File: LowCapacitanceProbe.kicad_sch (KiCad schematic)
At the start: 21 parts, among them J1 u.Fl, J5 u.Fl, Q1 BF998, U1 SPX3819M5-L

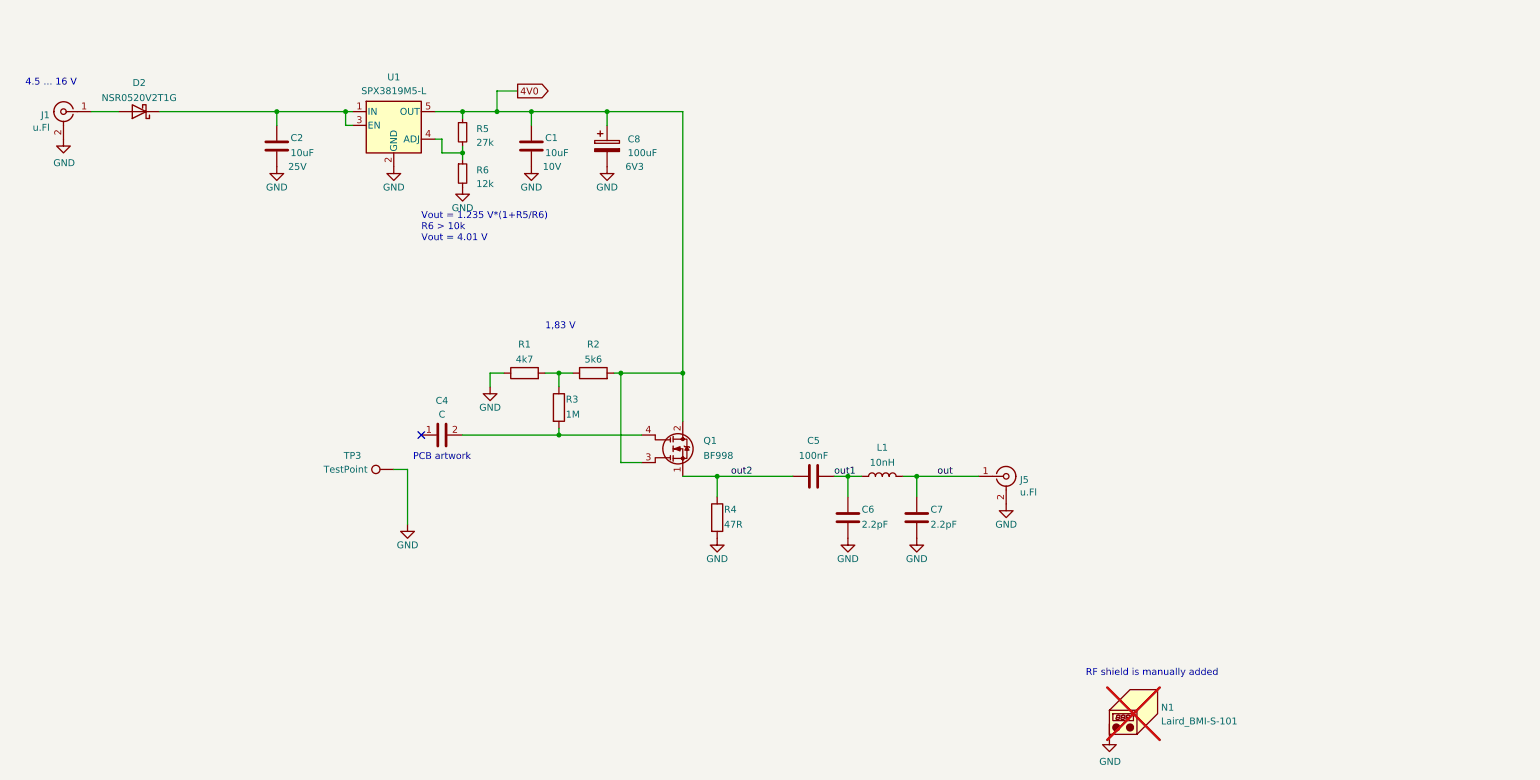
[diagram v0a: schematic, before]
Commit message: Slight fixes to simulation, started modifying schematics.
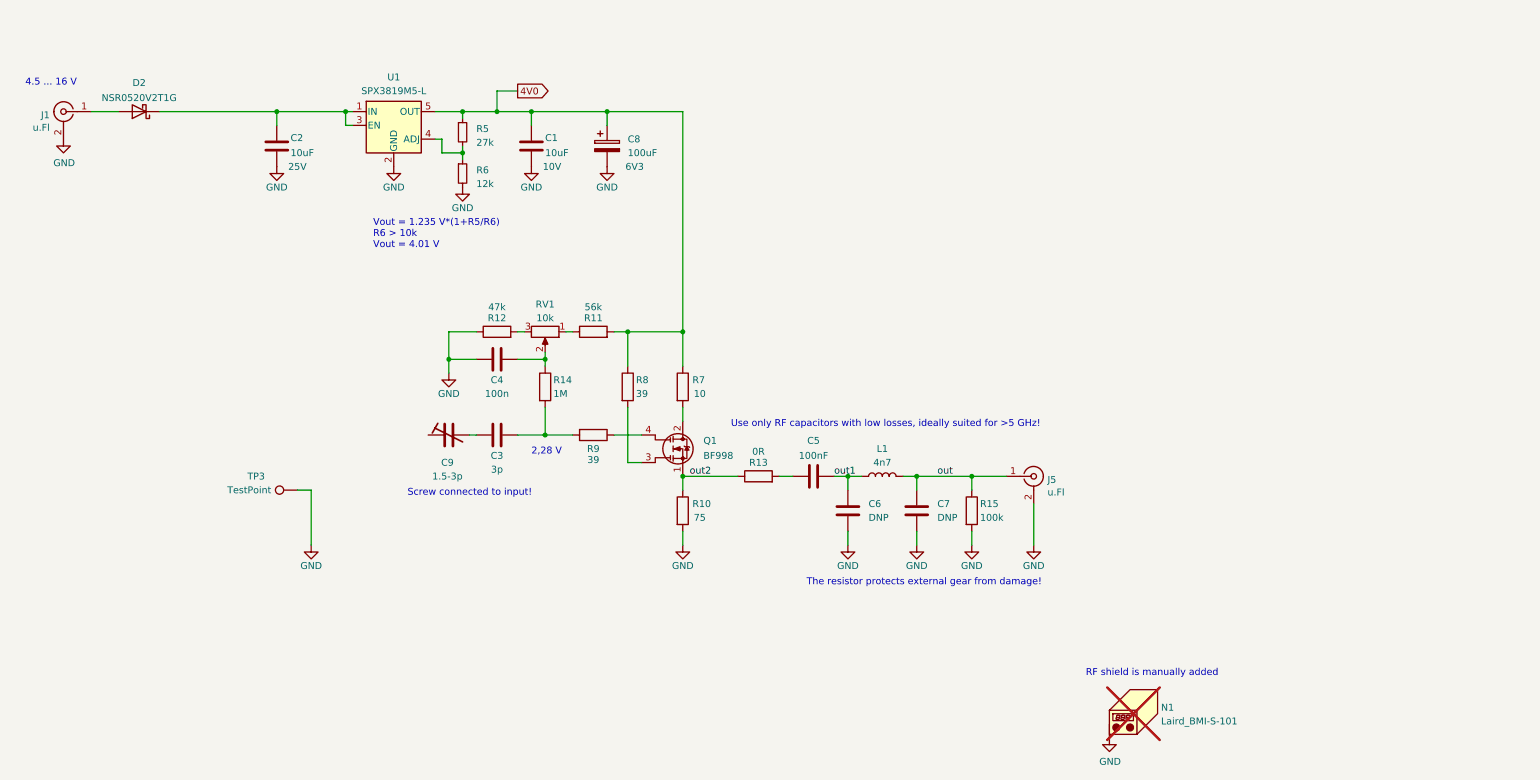
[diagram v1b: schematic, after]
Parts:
- removed R1: 4k7, Resistor_SMD:R_0402_1005Metric, symbol Device:R
- removed R2: 5k6, Resistor_SMD:R_0402_1005Metric, symbol Device:R
- removed R3: 1M, Resistor_SMD:R_0402_1005Metric, symbol Device:R
- removed R4: 47R, Resistor_SMD:R_0402_1005Metric, symbol Device:R
- added C3: 3p, symbol Device:C
- added C9: 1.5-3p, symbol Device:C_Trim
- added R10: 75, symbol Device:R
- added R11: 56k, symbol Device:R
- added R12: 47k, symbol Device:R
- added R13: 0R, symbol Device:R
- added R14: 1M, symbol Device:R
- added R15: 100k, symbol Device:R
- added R7: 10, symbol Device:R
- added R8, R9: 39, symbol Device:R
- added RV1: 10k, symbol Device:R_Potentiometer
- C4: value C -> 100n; footprint FETProbe:input_cap -> (none); now in the parts list
- C6, C7: value 2.2pF -> DNP; footprint FETProbe:C_0402_1005Metric_mod -> (none); LCSC Part C88927 -> (none); LCSC alternative C88887 -> (none); MPN RF15N2R2B500CT -> (none); OC_LCSC C172819 -> (none); dielectric NP0 -> (none)
- L1: value 10nH -> 4n7; footprint Inductor_SMD:L_0402_1005Metric -> (none); LCSC Part C90642 -> (none); MPN LQW15AN10NG80D -> (none)
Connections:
- net 4V0: now also R11.2, R7.1, R8.1; no longer Q1.2 (D), Q1.3 (G2)
- net GND: now also C4.2, R10.2, R12.1, R15.2
- net out: now also R15.1
- net out2: now also R10.1, R13.1; no longer C5.1
- net at Q1.4 (G1): now also R9.1; no longer C4.2
- net at C4.1: now also R14.1, RV1.2
- new net: C5.1, R13.2
- new net: Q1.2 (D), R7.2
- new net: Q1.3 (G2), R8.2
- new net: R11.1, RV1.1
- new net: R12.2, RV1.3
- new net: C3.1, C9.2
- new net: C3.2, R14.2, R9.2
- no-connect marks 1 -> 0
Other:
- note added: "2,28 V"
- note added: "Screw connected to input!"
- note added: "The resistor protects external gear from damage!"
- note added: "Use only RF capacitors with low losses, ideally suited for >5 GHz!"
- note removed: "1,83 V"
- note removed: "PCB artwork"
- moved on the sheet: J5, TP3

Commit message: Added more possibilities for tuning gain, added delinearization networks for easier fine-tuning, increased power supply voltage, fixed BF998 symbol. Added simulation of delinearization networks.
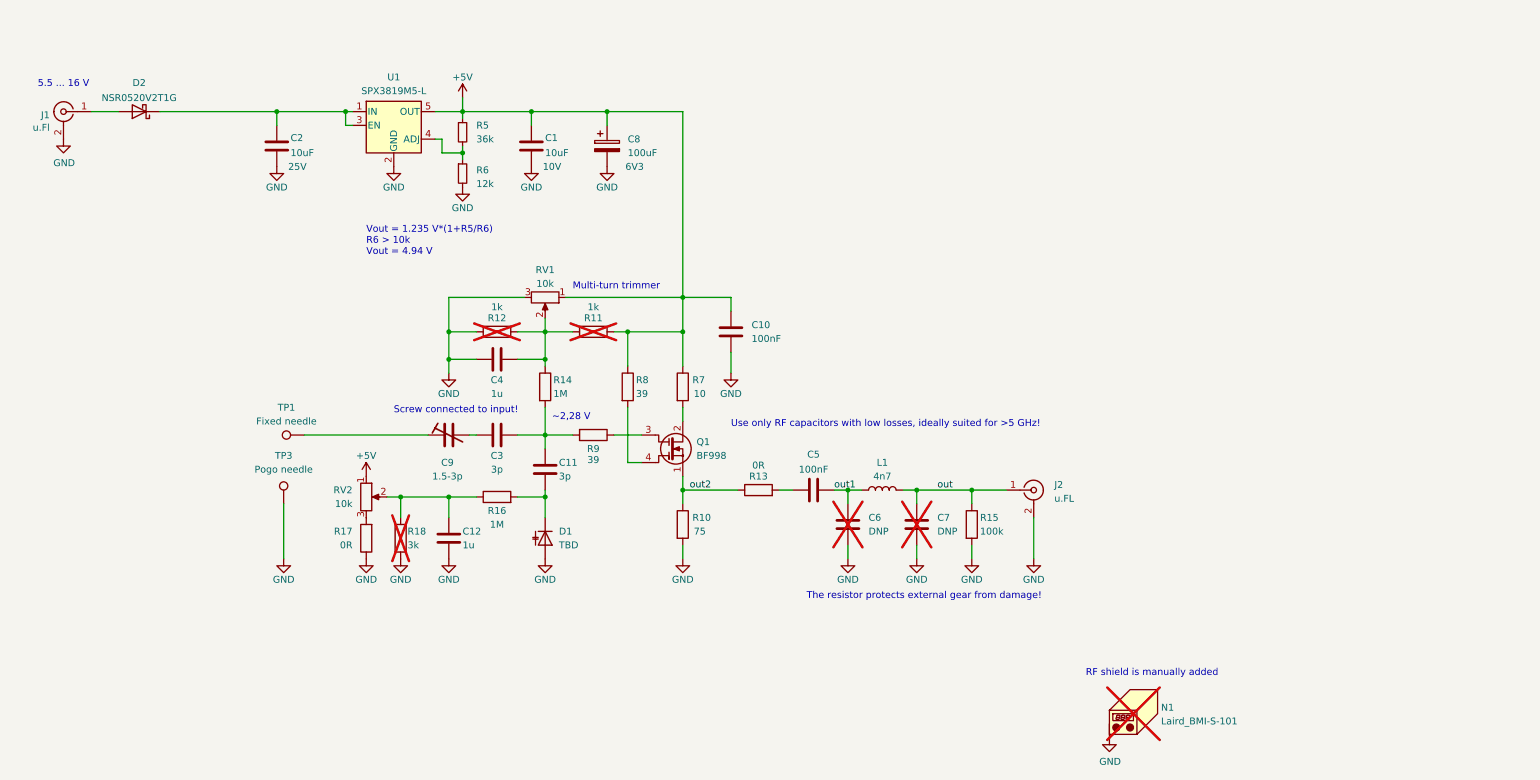
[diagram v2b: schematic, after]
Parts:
- removed J5: u.Fl, Connector_Coaxial:U.FL_Molex_MCRF_73412-0110_Vertical, symbol Connector:Conn_Coaxial
- removed Q1: BF998, FETProbe:SOT-143_mod, symbol BF998:BF998
- added C10: 100nF, Capacitor_SMD:C_1206_3216Metric, symbol Device:C
- added C11: 3p, symbol Device:C
- added C12: 1u, symbol Device:C
- added D1: TBD, symbol Device:D_Capacitance
- added J2: u.FL, Connector_Coaxial:U.FL_Molex_MCRF_73412-0110_Vertical, symbol petr:u.FL
- added Q1: BF998, Package_TO_SOT_SMD:SOT-143, symbol petr_kicad:BF998-petr_kicad_1
- added R16: 1M, symbol Device:R
- added R17: 0R, symbol Device:R
- added R18: 3k, symbol Device:R
- added RV2: 10k, symbol Device:R_Potentiometer
- added TP1: Fixed needle, symbol Connector:TestPoint
- C4: value 100n -> 1u
- C6, C7: now not fitted
- R11: value 56k -> 1k; now not fitted
- R12: value 47k -> 1k; now not fitted
- R5: value 27k -> 36k
- TP3: value TestPoint -> Pogo needle
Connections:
- net GND: now also RV1.3, C10.1, C12.2, D1.2 (A), J2.2 (Ext), R17.1, R18.1
- net out: now also J2.1 (In)
- net out2: now also Q1.1 (S)
- net at R7.2: now also Q1.2 (D)
- net at R8.2: now also Q1.4 (G2)
- net at R9.1: now also Q1.3 (G1)
- net at R11.1: now also C4.1, R12.2, R14.1, RV1.2; no longer RV1.1
- net at C3.2, R14.2, R9.2: now also C11.2
- net at C9.1: now also TP1.1
- net 4V0 renamed +5V
- net +5V: now also RV1.1, C10.2, RV2.1
- new net: C12.1, R16.1, R18.2, RV2.2
- new net: C11.1, D1.1 (K), R16.2
- new net: R17.2, RV2.3
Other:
- note added: "5.5 ... 16 V"
- note added: "Multi-turn trimmer"
- note added: "Vout = 1.235 V*(1+R5/R6) R6 > 10k Vout = 4.94 V"
- note added: "~2,28 V"
- note removed: "2,28 V"
- note removed: "4.5 ... 16 V"
- note removed: "Vout = 1.235 V*(1+R5/R6) R6 > 10k Vout = 4.01 V"
- moved on the sheet: C5, L1, R10, R13, R15, RV1, TP3

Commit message: Added calibration notes, fixed delinearization for gate bias
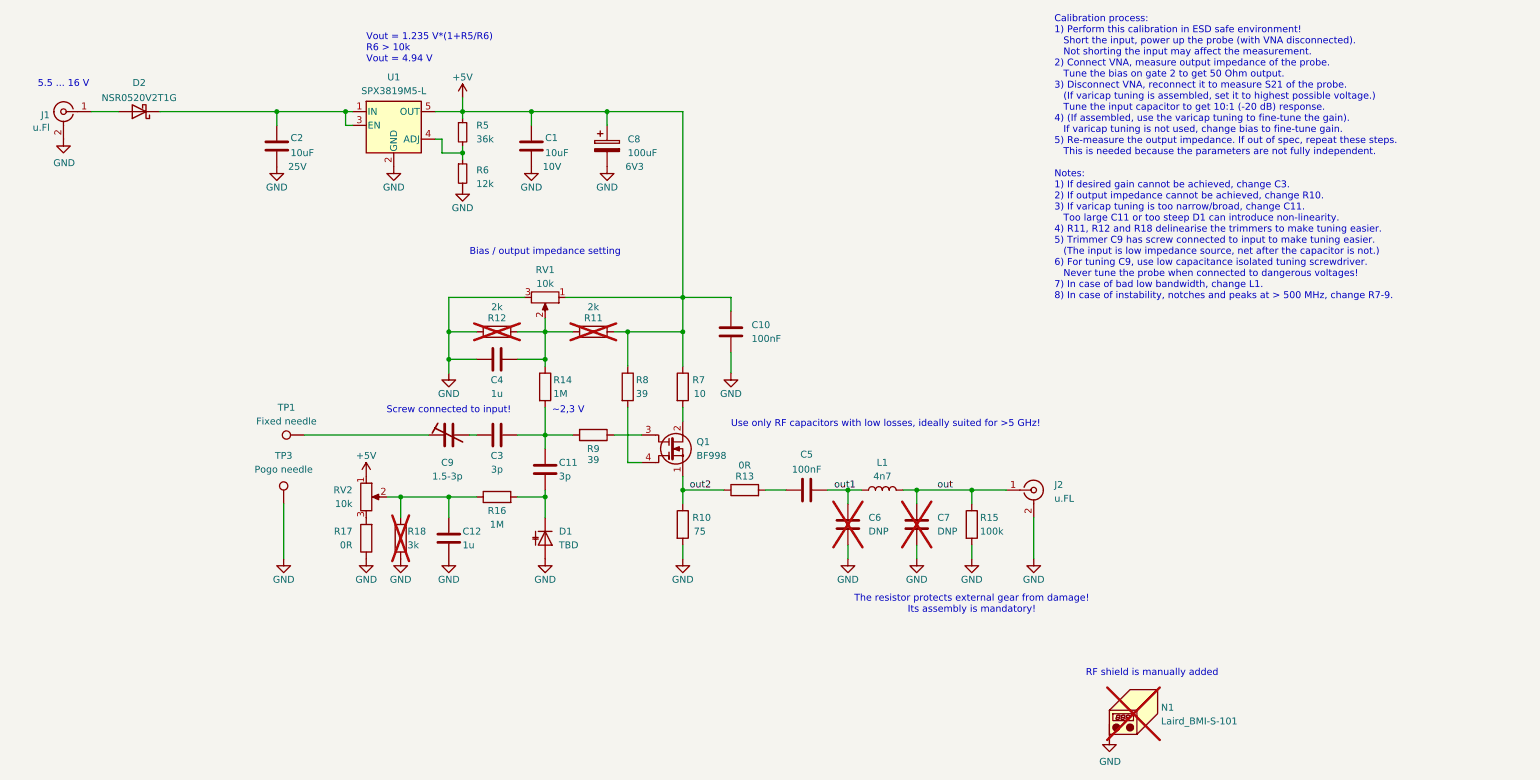
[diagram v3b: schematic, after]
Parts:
- R11, R12: value 1k -> 2k
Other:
- note added: "Bias / output impedance setting"
- note added: "Calibration process: 1) Perform this calibration in ESD safe environment! Short the input, power up the probe (with VNA disconnected). Not shorting the input may affect the measurement. 2) Connect VNA, measure output impedance of the probe. Tune the bias on gate 2 to get 50 Ohm output. 3) Disconnect VNA, reconnect it to measure S21 of the probe. (If varicap tuning is assembled, set it to highest 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"
- note added: "The resistor protects external gear from damage! Its assembly is mandatory!"
- note added: "~2,3 V"
- note removed: "Multi-turn trimmer"
- note removed: "The resistor protects external gear from damage!"
- note removed: "~2,28 V"
- moved on the sheet: C5, R13
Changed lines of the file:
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@@
 		)
 	)
-	(text "~2,28 V"
+	(text "~2,3 V"
 		(exclude_from_sim no)
-		(at 116.84 88.9 0)
+		(at 116.84 87.63 0)
 		(effects
 			(font
@@
 		)
 	)
-	(text "Multi-turn trimmer"
+	(text "The resistor protects external gear from damage!\nIts assembly is mandatory!"
 		(exclude_from_sim no)
-		(at 120.65 64.77 0)
+		(at 194.31 124.46 0)
 		(effects
 			(font
 				(size 1.27 1.27)
 			)
-			(justify left bottom)
+			(justify bottom)
 		)
 	)
-	(text "The resistor protects external gear from damage!"
+	(text "Bias / output impedance setting"
 		(exclude_from_sim no)
-		(at 163.83 121.92 0)
+		(at 115.57 58.42 0)
 		(effects
 			(font
 				(size 1.27 1.27)
 			)
-			(justify left bottom)
+			(justify bottom)
 		)
 	)
 	(text "Vout = 1.235 V*(1+R5/R6)\nR6 > 10k\nVout = 4.94 V"
 		(exclude_from_sim no)
-		(at 82.55 58.42 0)
+		(at 82.55 22.86 0)
 		(effects
 			(font
@@
 		)
 	)
+	(text "Calibration process:\n1) Perform this calibration in ESD safe environment!\n   Short the input, power up the probe (with VNA disconnected).\n   Not shorting the input may affect the measurement.\n2) Connect VNA, measure output impedance of the probe.\n   Tune the bias on gate 2 to get 50 Ohm output.\n3) Disconnect VNA, reconnect it to measure S21 of the probe.\n   (If varicap tuning is assembled, set it to highest possible voltage.)\n   Tune the input capacitor to get 10:1 (-20 dB) response.\n4) (If assembled, use the varicap tuning to fine-tune the gain).\n   If varicap tuning is not used, change bias to fine-tune gain.\n5) Re-measure the output impedance. If out of spec, repeat these steps.\n   This is needed because the parameters are not fully independent.\n   \nNotes:\n1) If desired gain cannot be achieved, change C3.\n2) If output impedance cannot be achieved, change R10.\n3) If varicap tuning is too narrow/broad, change C11.\n   Too large C11 or too steep D1 can introduce non-linearity.\n4) R11, R12 and R18 delinearise the trimmers to make tuning easier.\n5) Trimmer C9 has screw connected to input to make tuning easier.\n   (The input is low impedance source, net after the capacitor is not.)\n6) For tuning C9, use low capacitance isolated tuning screwdriver.\n   Never tune the probe when connected to dangerous voltages!\n7) In case of bad low bandwidth, change L1.\n8) In case of instability, notches and peaks at > 500 MHz, change R7-9."
+		(exclude_from_sim no)
+		(at 209.55 13.97 0)
+		(effects
+			(font
+				(size 1.27 1.27)
+			)
+			(justify left top)
+		)
+	)
 	(text "Screw connected to input!"
 		(exclude_from_sim no)
-		(at 87.63 87.63 0)
+		(at 97.79 87.63 0)
 		(effects
 			(font
 				(size 1.27 1.27)
 			)
-			(justify left bottom)
+			(justify bottom)
 		)
 	)
@@
 	(wire
 		(pts
-			(xy 158.75 101.6) (xy 161.29 101.6)
+			(xy 156.21 101.6) (xy 160.02 101.6)
 		)
 		(stroke
@@
 	(wire
 		(pts
-			(xy 140.97 101.6) (xy 151.13 101.6)
+			(xy 140.97 101.6) (xy 148.59 101.6)
 		)
 		(stroke
@@
 	(wire
 		(pts
-			(xy 168.91 101.6) (xy 171.45 101.6)
+			(xy 167.64 101.6) (xy 171.45 101.6)
 		)
 		(stroke
@@
 	(symbol
 		(lib_id "Device:R")
-		(at 154.94 101.6 90)
+		(at 152.4 101.6 90)
 		(unit 1)
 		(exclude_from_sim no)
@@
 		(dnp no)
 		(property "Reference" "R13"
-			(at 154.94 99.06 90)
+			(at 152.4 99.06 90)
 			(effects
 				(font
@@
 		)
 		(property "Value" "0R"
-			(at 154.94 97.028 90)
+			(at 152.4 97.028 90)
 			(effects
 				(font
@@
 		)
 		(property "Footprint" ""
-			(at 154.94 103.378 90)
+			(at 152.4 103.378 90)
 			(effects
 				(font
@@
 		)
 		(property "Datasheet" "~"
-			(at 154.94 101.6 0)
+			(at 152.4 101.6 0)
 			(effects
 				(font
@@
 		)
 		(property "Description" "Resistor"
-			(at 154.94 101.6 0)
+			(at 152.4 101.6 0)
 			(effects
 				(font
@@
 	(symbol
 		(lib_id "Device:C")
-		(at 165.1 101.6 90)
+		(at 163.83 101.6 90)
 		(unit 1)
 		(exclude_from_sim no)
@@
 		(dnp no)
 		(property "Reference" "C5"
-			(at 165.1 95.0149 90)
+			(at 163.83 95.0149 90)
 			(effects
 				(font
@@
 		)
 		(property "Value" "100nF"
-			(at 165.1 97.79 90)
+			(at 163.83 97.79 90)
 			(effects
 				(font
@@
 		)
 		(property "Footprint" "Capacitor_SMD:C_1206_3216Metric"
-			(at 168.91 100.6348 0)
+			(at 167.64 100.6348 0)
 			(effects
 				(font
@@
 		)
 		(property "Datasheet" "~"
-			(at 165.1 101.6 0)
+			(at 163.83 101.6 0)
 			(effects
 				(font
@@
 		)
 		(property "Description" ""
-			(at 165.1 101.6 0)
+			(at 163.83 101.6 0)
 			(effects
 				(font
@@
 		)
 		(property "dielectric" "NP0"
-			(at 165.1 101.6 0)
+			(at 163.83 101.6 0)
 			(effects
 				(font
@@
 		)
 		(property "MPN" "GRM3195C1H104GA05D"
-			(at 165.1 101.6 0)
+			(at 163.83 101.6 0)
 			(effects
 				(font
@@
 		)
 		(property "OC_LCSC" "C907944"
-			(at 165.1 101.6 0)
+			(at 163.83 101.6 0)
 			(effects
 				(font
@@
 		)
 		(property "LCSC Part" "C2981728"
-			(at 165.1 101.6 0)
+			(at 163.83 101.6 0)
 			(effects
 				(font
@@
 		)
 		(property "LCSC alternative" "C2981728"
-			(at 165.1 101.6 90)
+			(at 163.83 101.6 90)
 			(effects
 				(font
@@
 			)
 		)
-		(property "Value" "1k"
+		(property "Value" "2k"
 			(at 106.68 67.818 90)
 			(effects
@@
 			)
 		)
-		(property "Value" "1k"
+		(property "Value" "2k"
 			(at 124.46 67.818 90)
 			(effects
